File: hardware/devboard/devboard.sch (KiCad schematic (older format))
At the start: 59 parts

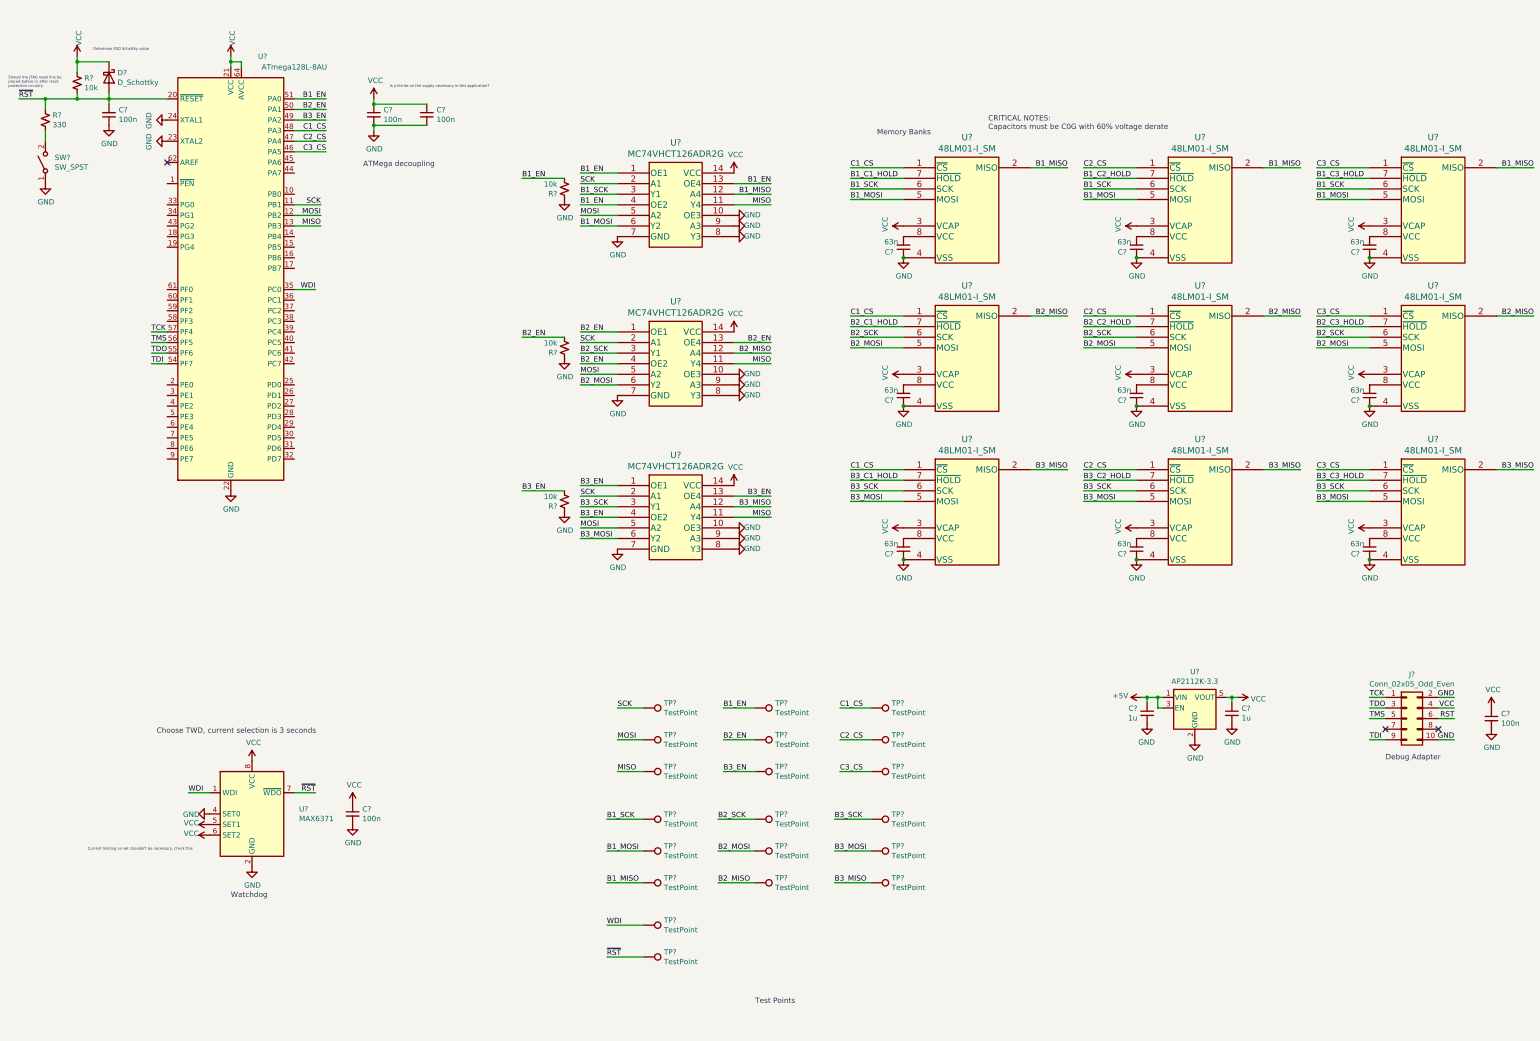
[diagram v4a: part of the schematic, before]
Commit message: Add breakout header
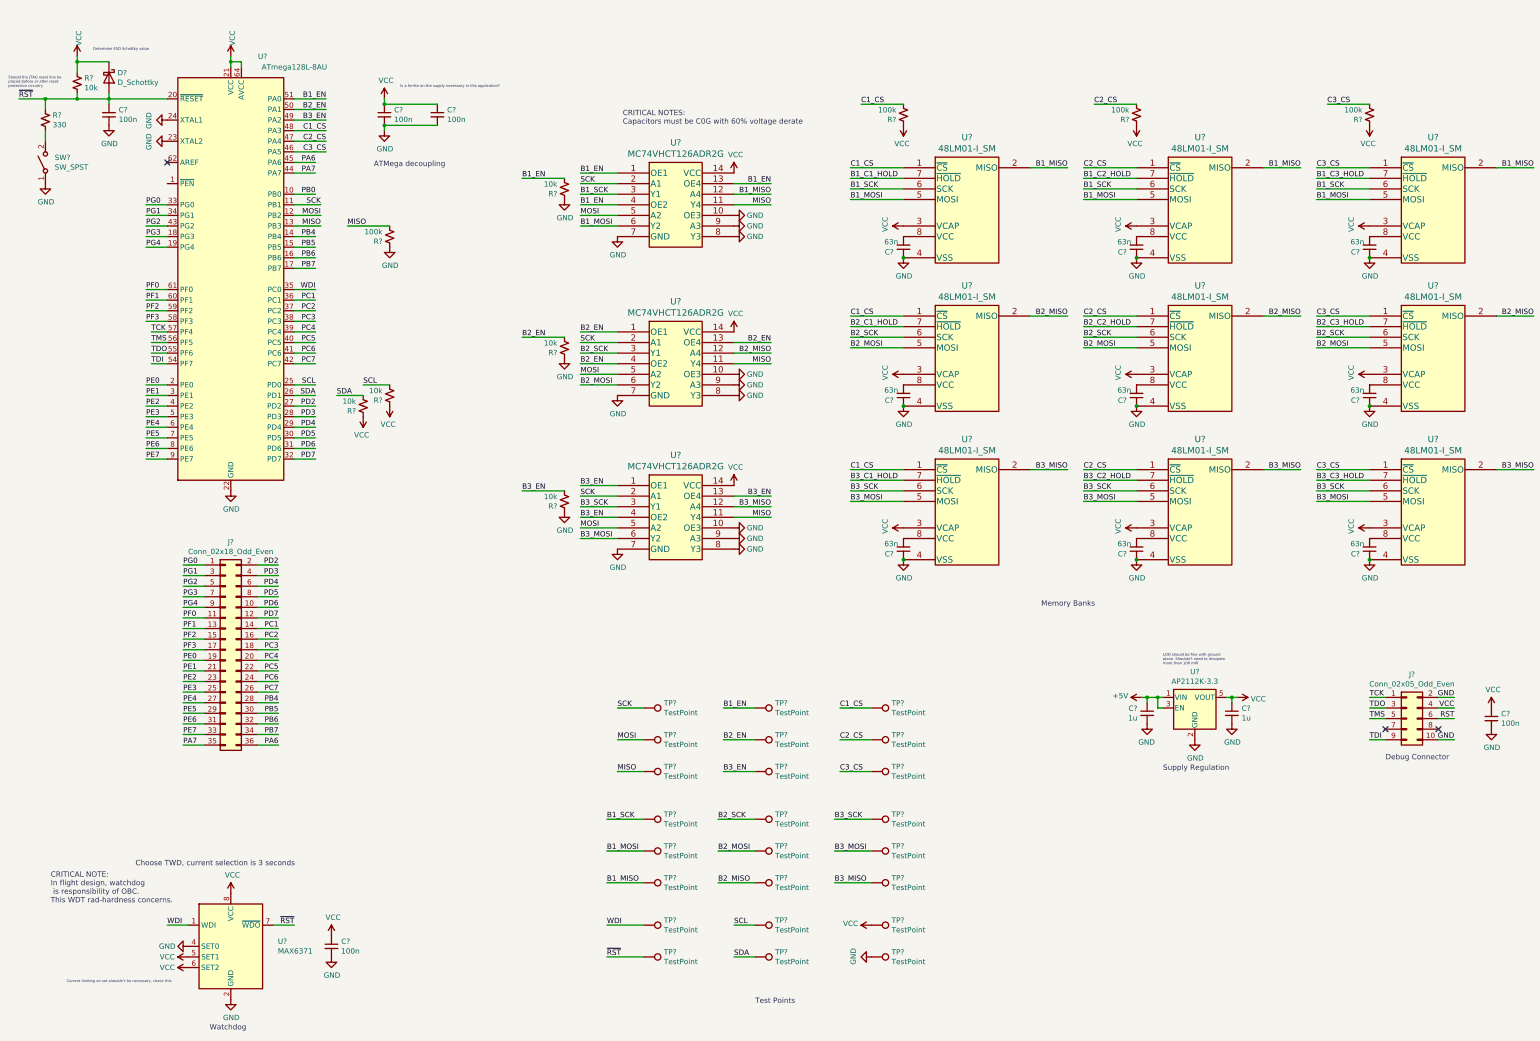
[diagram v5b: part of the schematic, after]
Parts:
- added J?: Conn_02x18_Odd_Even, Connector_PinHeader_2.54mm:PinHeader_2x18_P2.54mm_Vertical, symbol Connector_Generic:Conn_02x18_Odd_Even
- added R? (x2): 10k, symbol Device:R_Small_US
- added R? (x4): 100k, symbol Device:R_Small_US
- added TP? (x4): TestPoint, TestPoint:TestPoint_Bridge_Pitch2.54mm_Drill1.0mm, symbol Connector:TestPoint
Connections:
- net C1_CS: now also R?.2
- net C2_CS: now also R?.2
- net C3_CS: now also R?.2
- net GND: now also R?.1, TP?.1
- net MISO: now also R?.2
- net VCC: now also R?.1, R?.1, R?.1, R?.1, R?.1, TP?.1
- net PB0: now reaches U?.10 (PB0)
- net PB4: now reaches U?.14 (PB4)
- net PB4: now also J?.28 (Pin_28)
- net PB5: now reaches U?.15 (PB5)
- net PB5: now also J?.30 (Pin_30)
- net PB6: now reaches U?.16 (PB6)
- net PB6: now also J?.32 (Pin_32)
- net PB7: now reaches U?.17 (PB7)
- net PB7: now also J?.34 (Pin_34)
- net PG3: now reaches U?.18 (PG3)
- net PG3: now also J?.7 (Pin_7)
- net PG4: now reaches U?.19 (PG4)
- net PG4: now also J?.9 (Pin_9)
- net PE0: now reaches U?.2 (PE0)
- net PE0: now also J?.19 (Pin_19)
- net SCL: now reaches U?.25 (PD0)
- net SCL: now also R?.2, TP?.1
- net SDA: now reaches U?.26 (PD1)
- net SDA: now also R?.2, TP?.1
- net PD2: now reaches U?.27 (PD2)
- net PD2: now also J?.2 (Pin_2)
- net PD3: now reaches U?.28 (PD3)
- net PD3: now also J?.4 (Pin_4)
- net PD4: now reaches U?.29 (PD4)
- net PD4: now also J?.6 (Pin_6)
- net PE1: now reaches U?.3 (PE1)
- net PE1: now also J?.21 (Pin_21)
- net PD5: now reaches U?.30 (PD5)
- net PD5: now also J?.8 (Pin_8)
- net PD6: now reaches U?.31 (PD6)
- net PD6: now also J?.10 (Pin_10)
- net PD7: now reaches U?.32 (PD7)
- net PD7: now also J?.12 (Pin_12)
- net PG0: now reaches U?.33 (PG0)
- net PG0: now also J?.1 (Pin_1)
- net PG1: now reaches U?.34 (PG1)
- net PG1: now also J?.3 (Pin_3)
- net PC1: now reaches U?.36 (PC1)
- net PC1: now also J?.14 (Pin_14)
- net PC2: now reaches U?.37 (PC2)
- net PC2: now also J?.16 (Pin_16)
- net PC3: now reaches U?.38 (PC3)
- net PC3: now also J?.18 (Pin_18)
- net PC4: now reaches U?.39 (PC4)
- net PC4: now also J?.20 (Pin_20)
- net PE2: now reaches U?.4 (PE2)
- net PE2: now also J?.23 (Pin_23)
- net PC5: now reaches U?.40 (PC5)
- net PC5: now also J?.22 (Pin_22)
- net PC6: now reaches U?.41 (PC6)
- net PC6: now also J?.24 (Pin_24)
- net PC7: now reaches U?.42 (PC7)
- net PC7: now also J?.26 (Pin_26)
- net PG2: now reaches U?.43 (PG2)
- net PG2: now also J?.5 (Pin_5)
- net PA7: now reaches U?.44 (PA7)
- net PA7: now also J?.35 (Pin_35)
- net PA6: now reaches U?.45 (PA6)
- net PA6: now also J?.36 (Pin_36)
- net PE3: now reaches U?.5 (PE3)
- net PE3: now also J?.25 (Pin_25)
- net PF3: now reaches U?.58 (PF3)
- net PF3: now also J?.17 (Pin_17)
- net PF2: now reaches U?.59 (PF2)
- net PF2: now also J?.15 (Pin_15)
- net PE4: now reaches U?.6 (PE4)
- net PE4: now also J?.27 (Pin_27)
- net PF1: now reaches U?.60 (PF1)
- net PF1: now also J?.13 (Pin_13)
- net PF0: now reaches U?.61 (PF0)
- net PF0: now also J?.11 (Pin_11)
- net PE5: now reaches U?.7 (PE5)
- net PE5: now also J?.29 (Pin_29)
- net PE6: now reaches U?.8 (PE6)
- net PE6: now also J?.31 (Pin_31)
- net PE7: now reaches U?.9 (PE7)
- net PE7: now also J?.33 (Pin_33)
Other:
- note added: "CRITICAL NOTE:\nIn flight design, watchdog\n is responsibility of OBC.\nThis WDT rad-hardness concerns."
- note added: "Debug Connector"
- note added: "LDO should be fine with ground\nplane. Shouldn't need to dissipate\nmore than 100 mW"
- note added: "Supply Regulation"
- note removed: "Debug Adapter"
- moved on the sheet: C?, U?

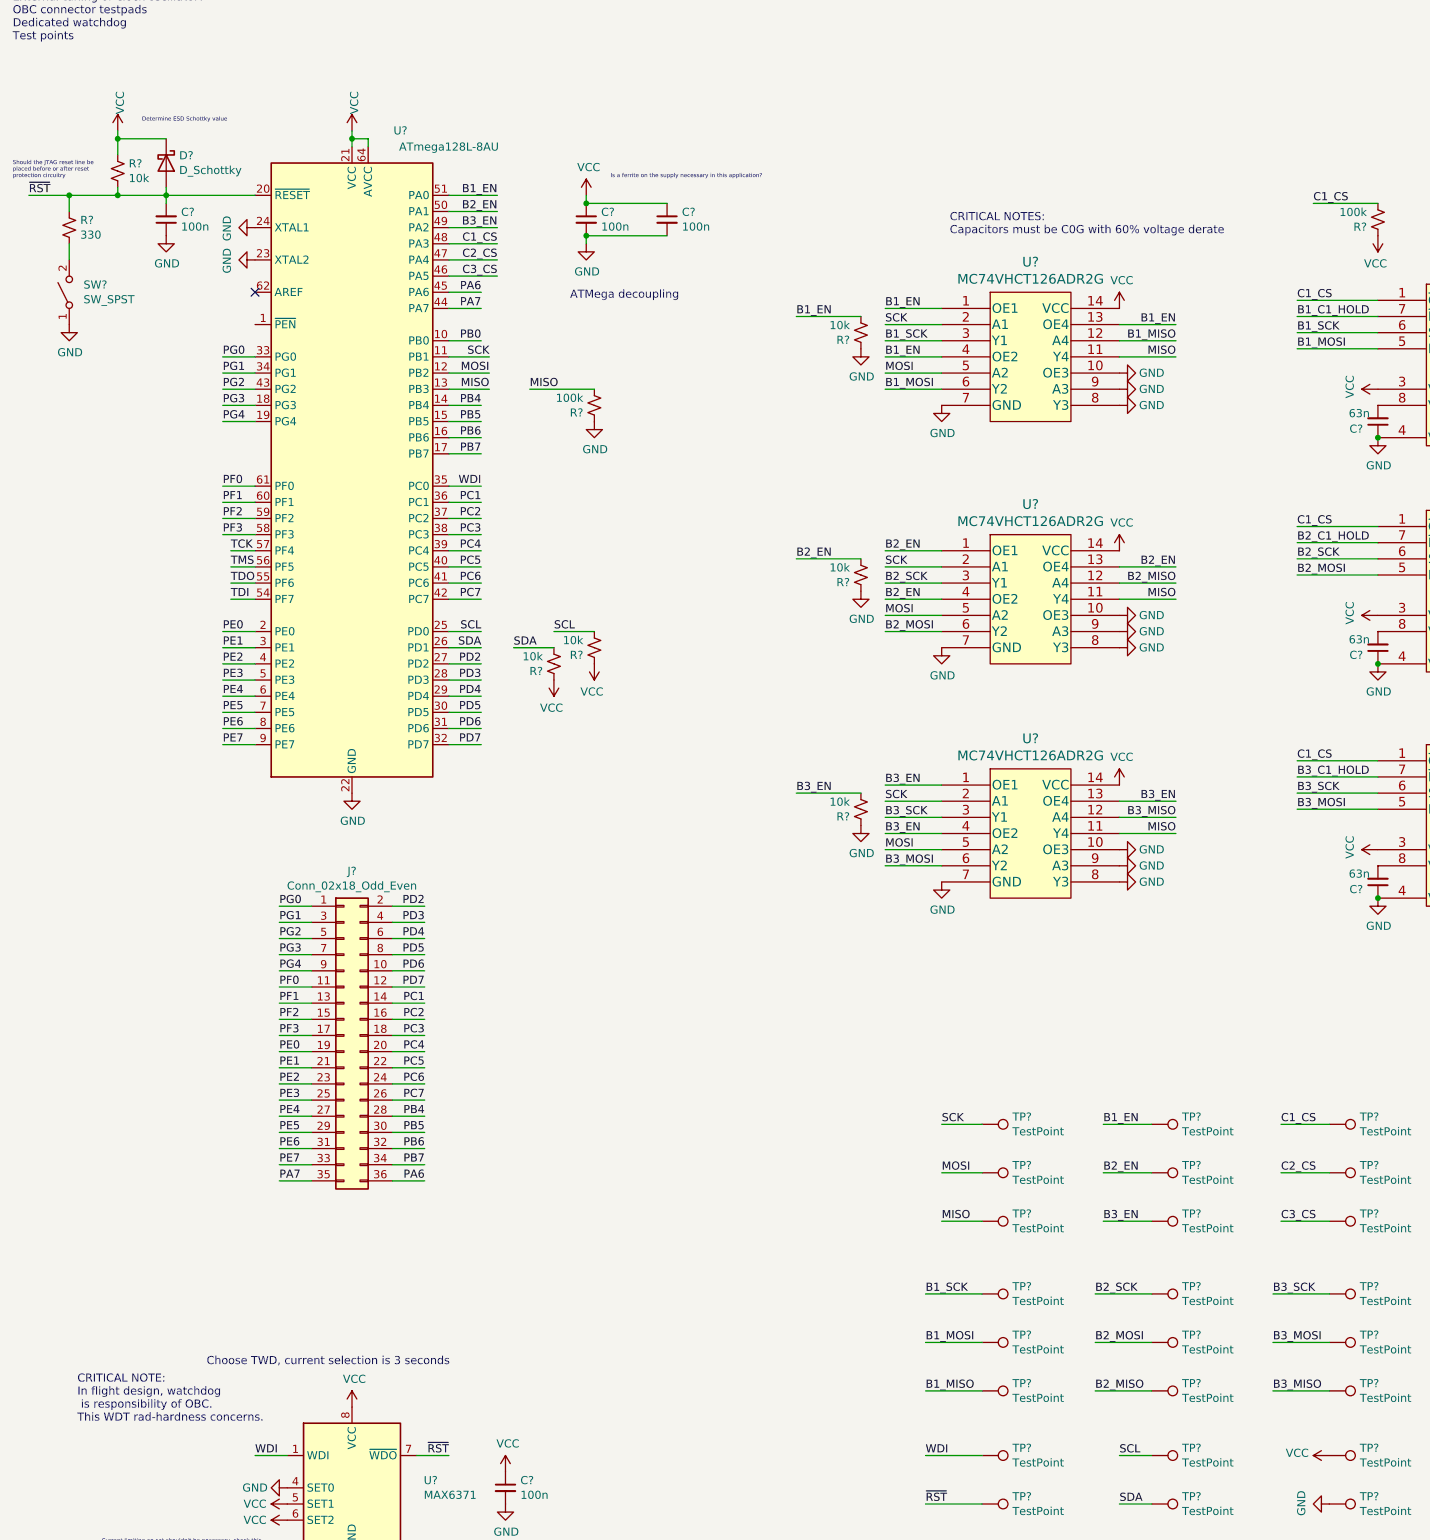
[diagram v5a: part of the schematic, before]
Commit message: Complete draft schematic
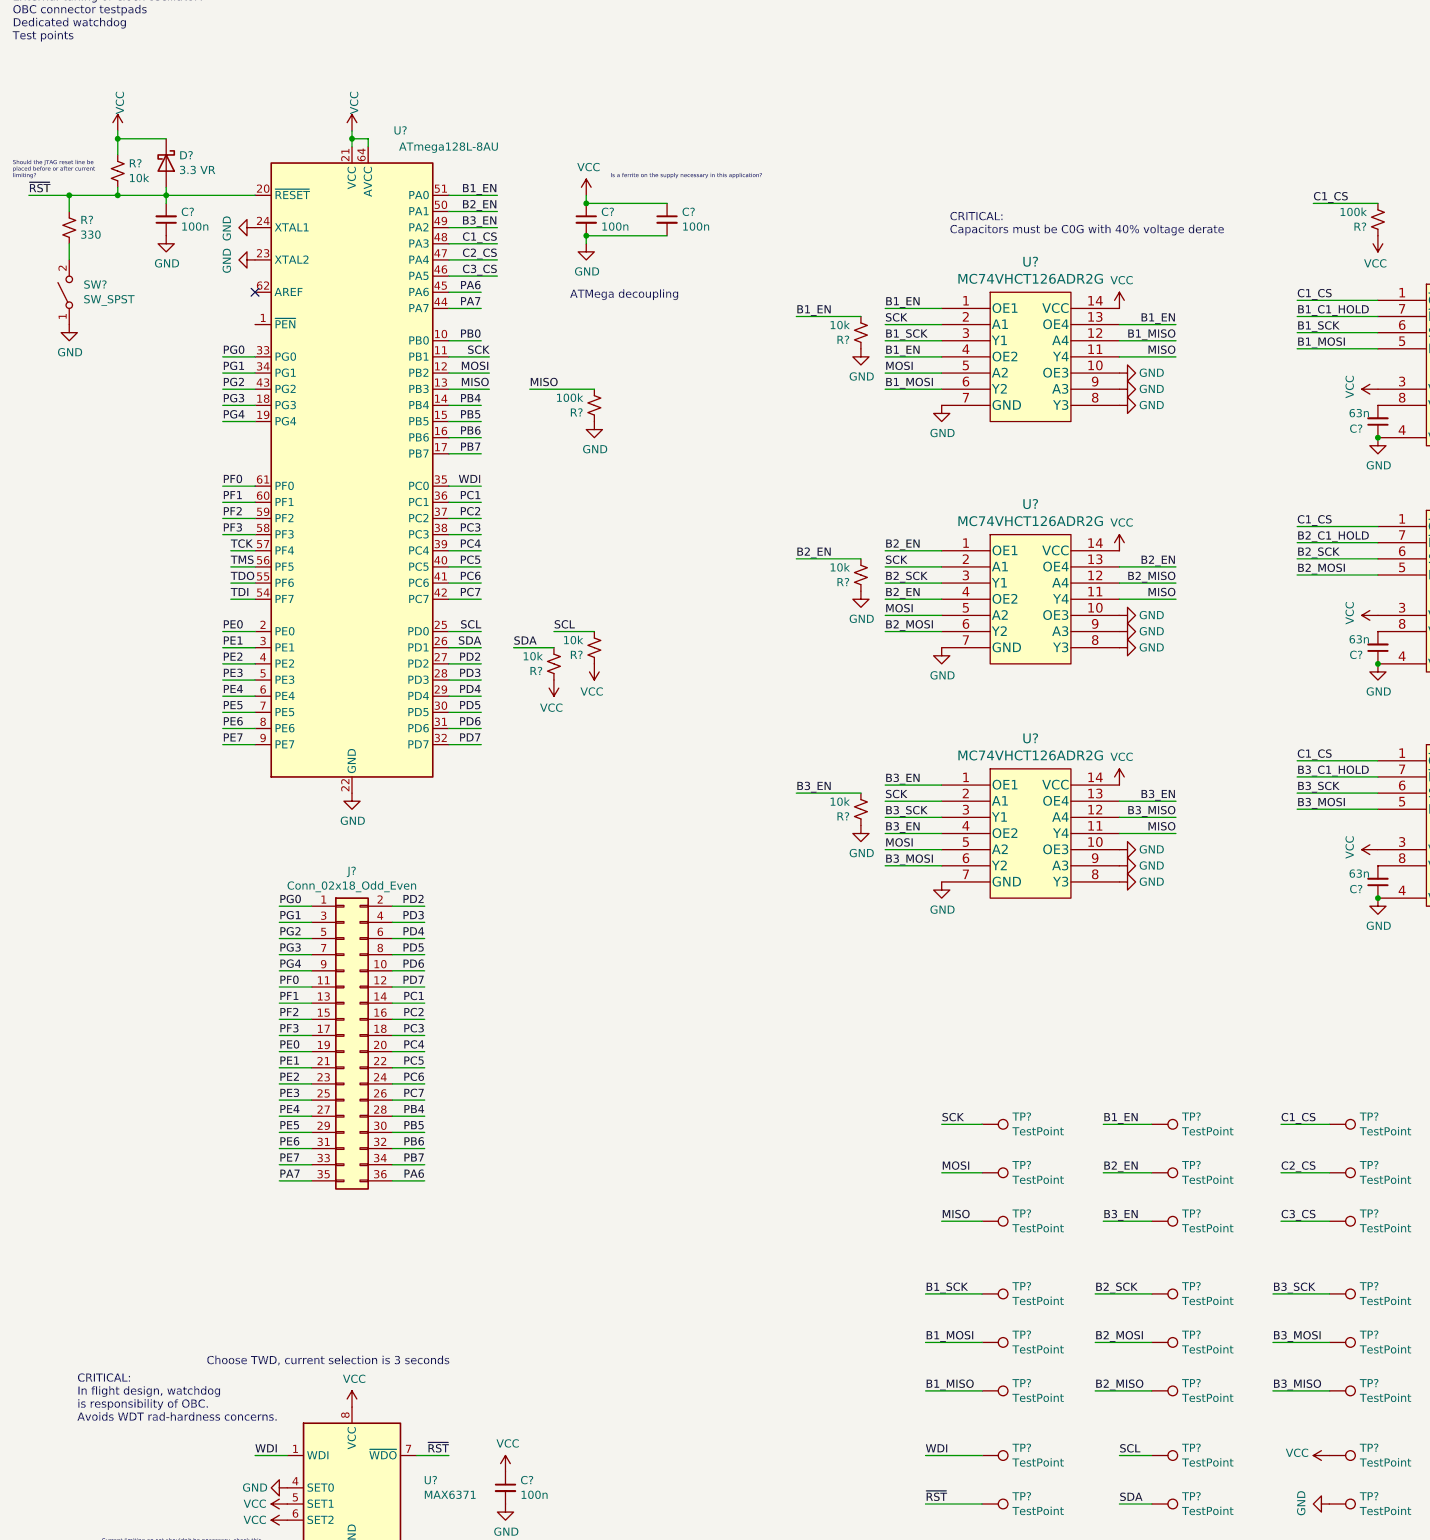
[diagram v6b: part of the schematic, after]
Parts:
- D?: value D_Schottky -> 3.3 VR
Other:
- note added: "CRITICAL:\nCapacitors must be C0G with 40% voltage derate"
- note added: "CRITICAL:\nIn flight design, watchdog\nis responsibility of OBC.\nAvoids WDT rad-hardness concerns."
- note added: "Should the JTAG reset line be\nplaced before or after current\nlimiting?"
- note removed: "CRITICAL NOTE:\nIn flight design, watchdog\n is responsibility of OBC.\nThis WDT rad-hardness concerns."
- note removed: "CRITICAL NOTES:\nCapacitors must be C0G with 60% voltage derate"
- note removed: "Determine ESD Schottky value"
- note removed: "Should the JTAG reset line be\nplaced before or after reset \nprotection circuitry"
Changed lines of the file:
@@
 $EndComp
 Text Notes 550  2100 0    25   ~ 0
-Should the JTAG reset line be\nplaced before or after reset \nprotection circuitry
-Text Notes 1350 1750 0    25   ~ 0
-Determine ESD Schottky value
+Should the JTAG reset line be\nplaced before or after current\nlimiting?
 Text Notes 550  1250 0    50   ~ 0
 CRITICAL ELEMENTS:\nMCU\nReset circuit\nDebug circuit\nExternal tuning or clock oscillator?\nOBC connector testpads\nDedicated watchdog\nTest points
@@
 $EndComp
 Text Notes 6350 2450 0    50   ~ 0
-CRITICAL NOTES:\nCapacitors must be C0G with 60% voltage derate
+CRITICAL:\nCapacitors must be C0G with 40% voltage derate
 Wire Wire Line
 	2650 1900 2650 1850
@@
 P 1500 2000
 F 0 "D?" V 1454 2080 50  0000 L CNN
-F 1 "D_Schottky" V 1545 2080 50  0000 L CNN
+F 1 "3.3 VR" V 1545 2080 50  0000 L CNN
 F 2 "" H 1500 2000 50  0001 C CNN
-F 3 "~" H 1500 2000 50  0001 C CNN
+F 3 "" H 1500 2000 50  0001 C CNN
 	1    1500 2000
 	0    1    1    0
@@
 	2200 8300 2400 8300
 Text Notes 950  9800 0    50   ~ 0
-CRITICAL NOTE:\nIn flight design, watchdog\n is responsibility of OBC.\nThis WDT rad-hardness concerns.
+CRITICAL:\nIn flight design, watchdog\nis responsibility of OBC.\nAvoids WDT rad-hardness concerns.
 $EndSCHEMATC

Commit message: Fix critical error
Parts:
- removed C? (x9): 63n, symbol Device:C_Small
- removed R?: 100k, symbol Device:R_Small_US
- added C? (x9): 68u, symbol Device:CP_Small
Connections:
- net GND: now also C?.2, C?.2, C?.2, C?.2, C?.2, C?.2, C?.2, C?.2, C?.2
- net VCC: now also U?.8 (VCC), U?.8 (VCC), U?.8 (VCC), U?.8 (VCC), U?.8 (VCC), U?.8 (VCC), U?.8 (VCC), U?.8 (VCC), U?.8 (VCC); no longer U?.3 (VCAP), U?.3 (VCAP), U?.3 (VCAP), U?.3 (VCAP), U?.3 (VCAP), U?.3 (VCAP), U?.3 (VCAP), U?.3 (VCAP), U?.3 (VCAP)
- new net: C?.1, U?.3 (VCAP) (x9)
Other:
- note added: "CRITICAL:\nCapacitors must be Tantalum with >40% voltage derate"
- note removed: "CRITICAL:\nCapacitors must be C0G with 40% voltage derate"
- moved on the sheet: R?
